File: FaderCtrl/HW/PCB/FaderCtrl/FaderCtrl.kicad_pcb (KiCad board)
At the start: 4 copper layers, 123 x 100 mm, 110 parts, among them J1 UART, J10 MP4, J2 PDI, J3 PORTE, J4 VBAT, J5 Barrel_Jack_MountingPin, J6 PWM, J7 MP1, J8 MP2, J9 MP3, P1 USB_C_Plug_USB2.0, SW1 BTN1, SW2 BTN2, SW3 BTN3, U1 ATxmega256A3BU-A, U2 TSR_1-2450, U3 AMS1117-3.3, Y1 32k, Y2 12M

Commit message: layout progress on FaderCtrl
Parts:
- removed NT1: GNDD, NetTie:NetTie-2_SMD_Pad0.5mm
- removed P1: USB_C_Plug_USB2.0, Connector_USB:USB_C_Receptacle_GCT_USB4125-xx-x-0190_6P_TopMnt_Horizontal
- removed R2: 56k, Resistor_SMD:R_0603_1608Metric_Pad0.98x0.95mm_HandSolder
- removed R3: 5k1, Resistor_SMD:R_0603_1608Metric_Pad0.98x0.95mm_HandSolder
- removed TP2: Vconn, TestPoint:TestPoint_Pad_D1.0mm
- added J11: USB_B_Mini, Connector_USB:USB_Mini-B_Wuerth_65100516121_Horizontal, B.Cu at (100.5, 116.6)
- added MPM1: PSM01081A103B2_MotorOnly, Connector_JST:JST_XH_B2B-XH-A_1x02_P2.50mm_Vertical, F.Cu at (43.4, 84.5)
- added MPM2: PSM01081A103B2_MotorOnly, Connector_JST:JST_XH_B2B-XH-A_1x02_P2.50mm_Vertical, F.Cu at (34.3, 84.5)
- added MPM3: PSM01081A103B2_MotorOnly, Connector_JST:JST_XH_B2B-XH-A_1x02_P2.50mm_Vertical, F.Cu at (43.2, 134.5)
- added MPM4: PSM01081A103B2_MotorOnly, Connector_JST:JST_XH_B2B-XH-A_1x02_P2.50mm_Vertical, F.Cu at (34.2, 134.5)
- C1, C10, C11, C12, C14, C15, C18, C19, C2, C20, C24, C25, C26, C27, C28, C29, C3, C30, C31, C32, C33, C34, C35, C36, C37, C38, C39, C4, C40, C42, C43, C5, C7, C8, C9, D1, J1, J3, J4, J6, JP1, JP2, NT2, R1, R10, R11, R12, R13, R4, R5, R6, R7, R8, R9, U1, U3, U4, U5, Y1, Y2: moved to B.Cu
- D2, D4, D6, D7: footprint Package_TO_SOT_SMD:SOT-323_SC-70 -> Package_TO_SOT_SMD:SOT-23_Handsoldering; moved to B.Cu
- MP1, MP2, MP3, MP4: footprint footprints:PSM01-082A-103B2_MotorizedPot -> Connector_JST:JST_XH_B7B-XH-A_1x07_P2.50mm_Vertical
- TP3, TP8, TP9: moved to F.Cu
- TP4: footprint TestPoint:TestPoint_Pad_D1.0mm -> TestPoint:TestPoint_THTPad_D1.0mm_Drill0.5mm
- moved R7 225.4 mm to (103.4, 131.0), turned to 90 degrees
- moved R6 223.5 mm to (91.4, 133.8), turned to 0 degrees
- moved J5 223.4 mm to (94.7, 144.9), turned to 180 degrees
- moved J3 221.7 mm to (91.9, 127.0), turned to 90 degrees
- moved R5 219.2 mm to (76.7, 134.0), turned to 0 degrees
- moved J2 217.2 mm to (62.0, 142.7), turned to -90 degrees
- moved U2 216.3 mm to (89.8, 147.4), turned to 90 degrees
- moved R4 215.7 mm to (61.5, 134.0), turned to 0 degrees
- moved C16 215.4 mm to (87.4, 147.4), turned to 90 degrees
- moved C21 214.0 mm to (85.4, 147.0), turned to 90 degrees
- moved TP5 210.6 mm to (62.6, 131.6), turned to 0 degrees
- moved C23 208.7 mm to (87.4, 144.0), turned to -90 degrees
- moved JP1 204.5 mm to (83.4, 142.2), turned to 90 degrees
- moved R1 201.6 mm to (57.9, 140.5)
- moved C3 200.2 mm to (83.8, 121.2)
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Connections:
- C1 pad 2: GNDD -> GND
- C13 pad 2: GNDD -> GND
- C17 pad 2: GNDD -> GND
- C2 pad 2: GNDD -> GND
- C22 pad 2: GNDD -> GND
- C26 pad 2: GNDD -> GND
- C28 pad 2: GNDD -> GND
- C29 pad 2: GNDD -> GND
- C3 pad 2: GNDD -> GND
- C32 pad 2: GNDD -> GND
- C35 pad 2: GNDD -> GND
- C36 pad 2: GNDD -> GND
- C37 pad 2: GNDD -> GND
- C38 pad 2: GNDD -> GND
- C39 pad 2: GNDD -> GND
- C4 pad 2: GNDD -> GND
- D3 pad 3: GNDD -> GND
- D3 pad 4: GNDD -> GND
- D5 pad 3: GNDD -> GND
- D5 pad 4: GNDD -> GND
- J1 pad 3: GNDD -> GND
- J2 pad 6: GNDD -> GND
- J3 pad 8: GNDD -> GND
- J4 pad 2: GNDD -> GND
- J5 pad 3: (no net) -> GND
- J6 pad 1: GNDD -> GND
- MP1 pad 1: /M1A -> /MP4P
- MP1 pad 2: /M1B -> /MP4S
- MP1 pad 3: /MP4P -> /MP4N
- MP1 pad 4: /MP4S -> /TP1
- MP1 pad 5: /MP4N -> VDDA
- MP1 pad 6: /TP1 -> /TR1
- MP1 pad 7: VDDA -> GNDA
- MP2 pad 1: /M2A -> /MP3P
- MP2 pad 2: /M2B -> /MP3S
- MP2 pad 3: /MP3P -> /MP3N
- MP2 pad 4: /MP3S -> /TP2
- MP2 pad 5: /MP3N -> VDDA
- MP2 pad 6: /TP2 -> /TR2
- MP2 pad 7: VDDA -> GNDA
- MP3 pad 1: /M3A -> /MP2P
- MP3 pad 2: /M3B -> /MP2S
- MP3 pad 3: /MP2P -> /MP2N
- MP3 pad 4: /MP2S -> /TP3
- MP3 pad 5: /MP2N -> VDDA
- MP3 pad 6: /TP3 -> /TR3
- MP3 pad 7: VDDA -> GNDA
- MP4 pad 1: /M4A -> /MP1P
- MP4 pad 2: /M4B -> /MP1S
- MP4 pad 3: /MP1P -> /MP1N
- MP4 pad 4: /MP1S -> /TP4
- MP4 pad 5: /MP1N -> VDDA
- MP4 pad 6: /TP4 -> /TR4
- MP4 pad 7: VDDA -> GNDA
- NT2 pad 1: GNDD -> GND
- SW1 pad 1: GNDD -> GND
- SW2 pad 1: GNDD -> GND
- SW3 pad 1: GNDD -> GND
- U1 pad 14: GNDD -> GND
- U1 pad 24: GNDD -> GND
- U1 pad 34: GNDD -> GND
- U1 pad 44: GNDD -> GND
- U1 pad 52: GNDD -> GND
- U1 pad 60: GNDD -> GND
- U3 pad 1: GNDD -> GND
- U4 pad 20: GNDD -> GND
- U5 pad 20: GNDD -> GND
- Y1 pad 3: GNDD -> GND
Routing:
- net VDDA: track 3.03 -> 162.8 mm
- net GND: track 0.00 -> 152.5 mm, vias 0 -> 5
- net /~{OE}: track 0.00 -> 87.8 mm, vias 0 -> 2
- net GNDA: track 0.00 -> 81.8 mm
- net VDD: track 18.5 -> 91.6 mm
- net /TP2: track 0.00 -> 68.8 mm, vias 0 -> 2
- net /PDI_CLK: track 0.00 -> 63.6 mm, vias 0 -> 1
- net /PDI_DATA: track 0.00 -> 57.9 mm, vias 0 -> 1
- net /M3A: track 0.00 -> 42.1 mm
- net /M1A: track 0.00 -> 41.9 mm
- net Vdrive: track 0.00 -> 30.7 mm, vias 0 -> 3
- net /M2A: track 0.00 -> 23.9 mm
- net /XTAL2: track 0.00 -> 23.4 mm
- net /M4A: track 0.00 -> 23.4 mm
- net /Cb4H: track 0.00 -> 16.9 mm
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- added copper zone on B.Cu, net GND
- added copper zone on F.Cu, net GND
- added copper zone on In1.Cu, net GND
- added copper zone on In2.Cu, net GND
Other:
- board size 123 x 100 mm -> 75 x 100 mm

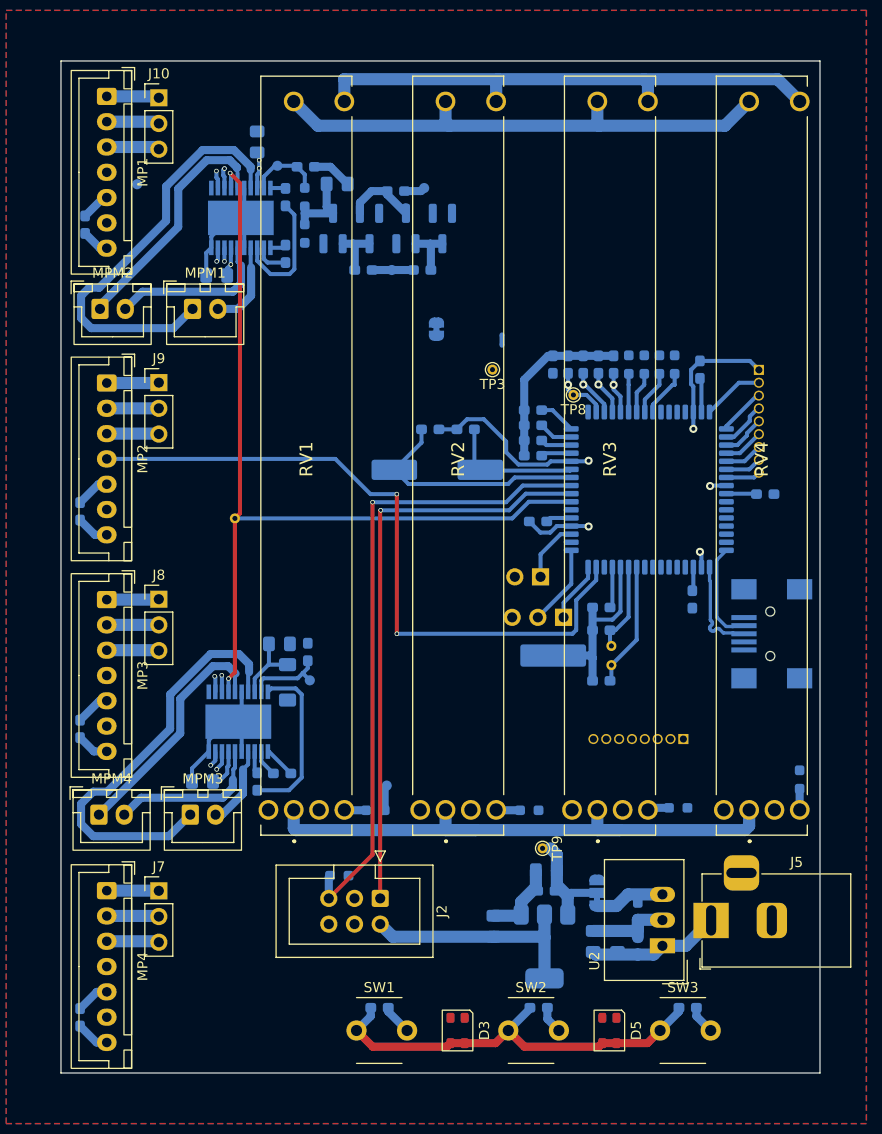
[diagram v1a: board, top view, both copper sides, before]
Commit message: layout fader done
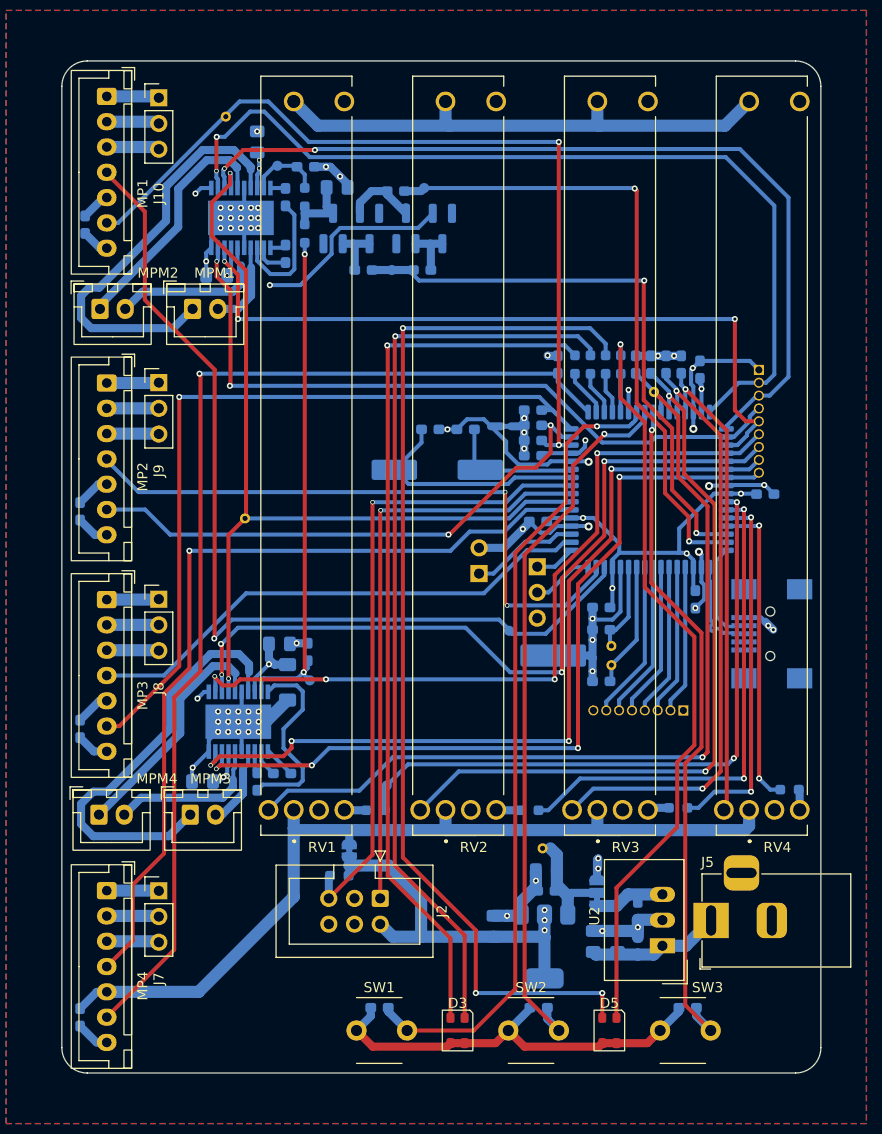
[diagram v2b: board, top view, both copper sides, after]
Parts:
- TP3, TP8, TP9: moved to B.Cu
- moved TP1 57.4 mm to (74.7, 116.3)
- moved JP2 52.3 mm to (58.9, 138.1), turned to 90 degrees
- moved TP3 36.3 mm to (46.7, 65.5), turned to 0 degrees
- moved NT2 8.53 mm to (74.4, 96.1), turned to 0 degrees
- moved TP8 7.96 mm to (89.0, 92.7)
- moved C14 6.68 mm to (87.2, 90.0)
- moved C15 6.68 mm to (88.7, 90.0)
- moved C19 6.68 mm to (90.2, 90.0)
- moved C20 6.68 mm to (91.7, 90.0)
- moved J4 6.08 mm to (71.7, 110.7), turned to 0 degrees
- moved J1 5.64 mm to (77.5, 110.0), turned to 180 degrees
- moved R10 5.32 mm to (84.2, 90.0)
- moved R11 5.32 mm to (85.7, 90.0)
- moved R8 5.32 mm to (81.2, 90.0)
- moved R9 5.32 mm to (82.7, 90.0)
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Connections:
- J1 pad 1: /RXD -> /TXD
- J1 pad 2: /TXD -> /RXD
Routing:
- net VDD: track 91.6 -> 312.2 mm, vias 0 -> 10
- net GNDA: track 81.8 -> 243.1 mm, vias 0 -> 6
- net Vdrive: track 30.7 -> 186.7 mm, vias 3 -> 6
- net /TR4: track 0.00 -> 108.1 mm, vias 0 -> 1
- net Net-(D5-A2): track 0.00 -> 105.5 mm, vias 0 -> 3
- net /TP1: track 0.00 -> 94.2 mm, vias 0 -> 1
- net Net-(D3-A1): track 0.00 -> 90.8 mm, vias 0 -> 1
- net Net-(D3-A2): track 0.00 -> 88.0 mm, vias 0 -> 1
- net VDDA: track 162.8 -> 249.2 mm, vias 0 -> 2
- net /TP4: track 0.00 -> 83.9 mm, vias 0 -> 1
- net /SL1: track 5.74 -> 88.4 mm
- net /PWM1A: track 7.82 -> 89.6 mm, vias 1 -> 2
- net /TR1: track 3.11 -> 84.3 mm, vias 0 -> 2
- net /PWM1B: track 6.80 -> 86.7 mm, vias 1 -> 2
- net /BTN1: track 3.02 -> 80.0 mm, vias 0 -> 1
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- added copper zone on In2.Cu, net VDD
- added copper zone on In2.Cu, net Vdrive
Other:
- outline, holes or cut-outs redrawn
- board text added: "1"
- board text added: "2"
- board text added: "3"
- board text added: "4"
- board text added: "G"
- board text added: "TX RX G"
- board text added: "V 0 5 G"
